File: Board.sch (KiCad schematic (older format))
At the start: 0 parts

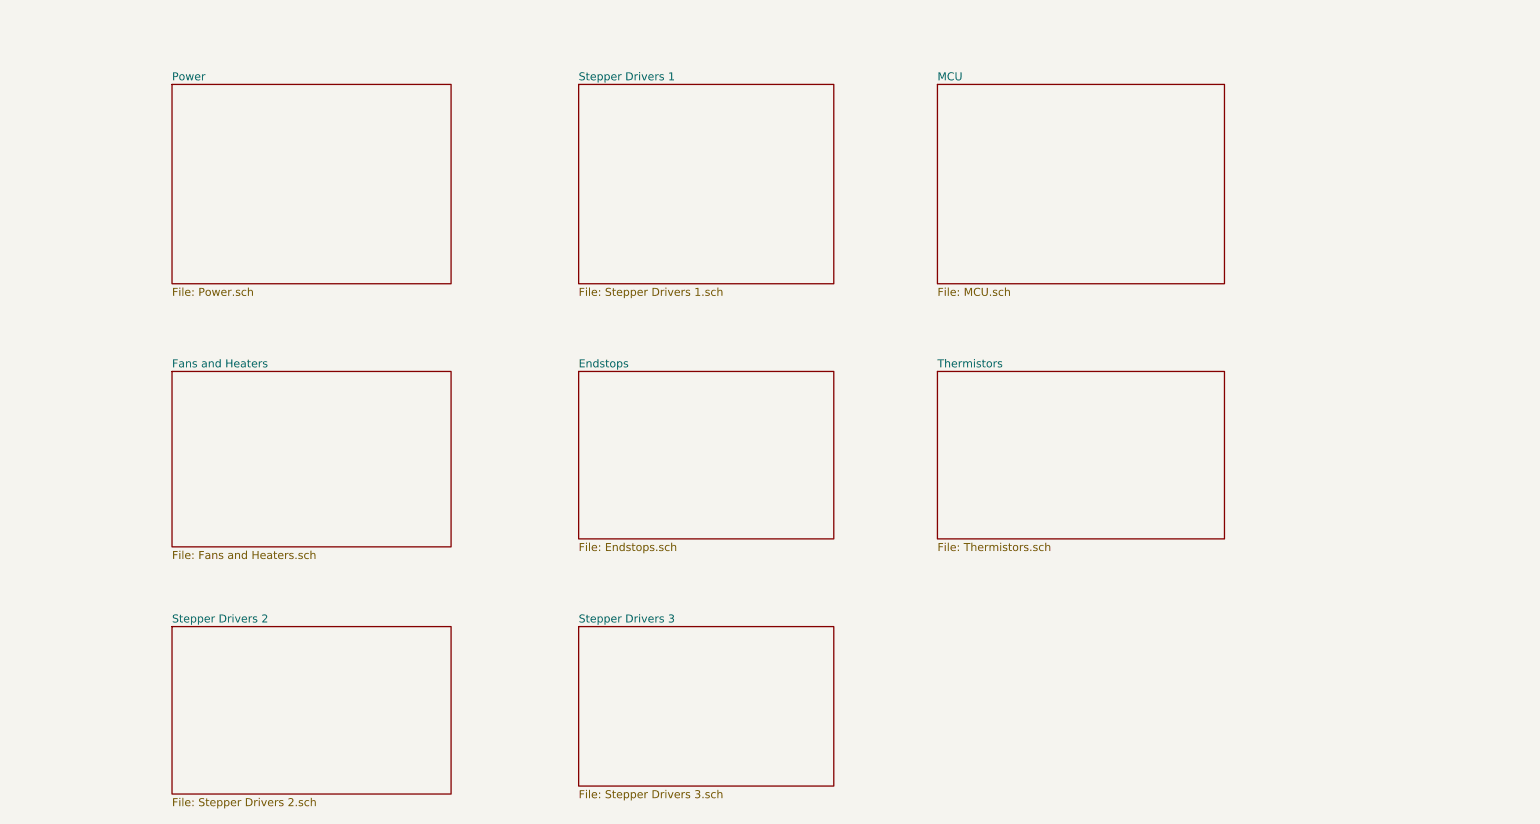
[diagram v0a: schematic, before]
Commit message: Added more footprints
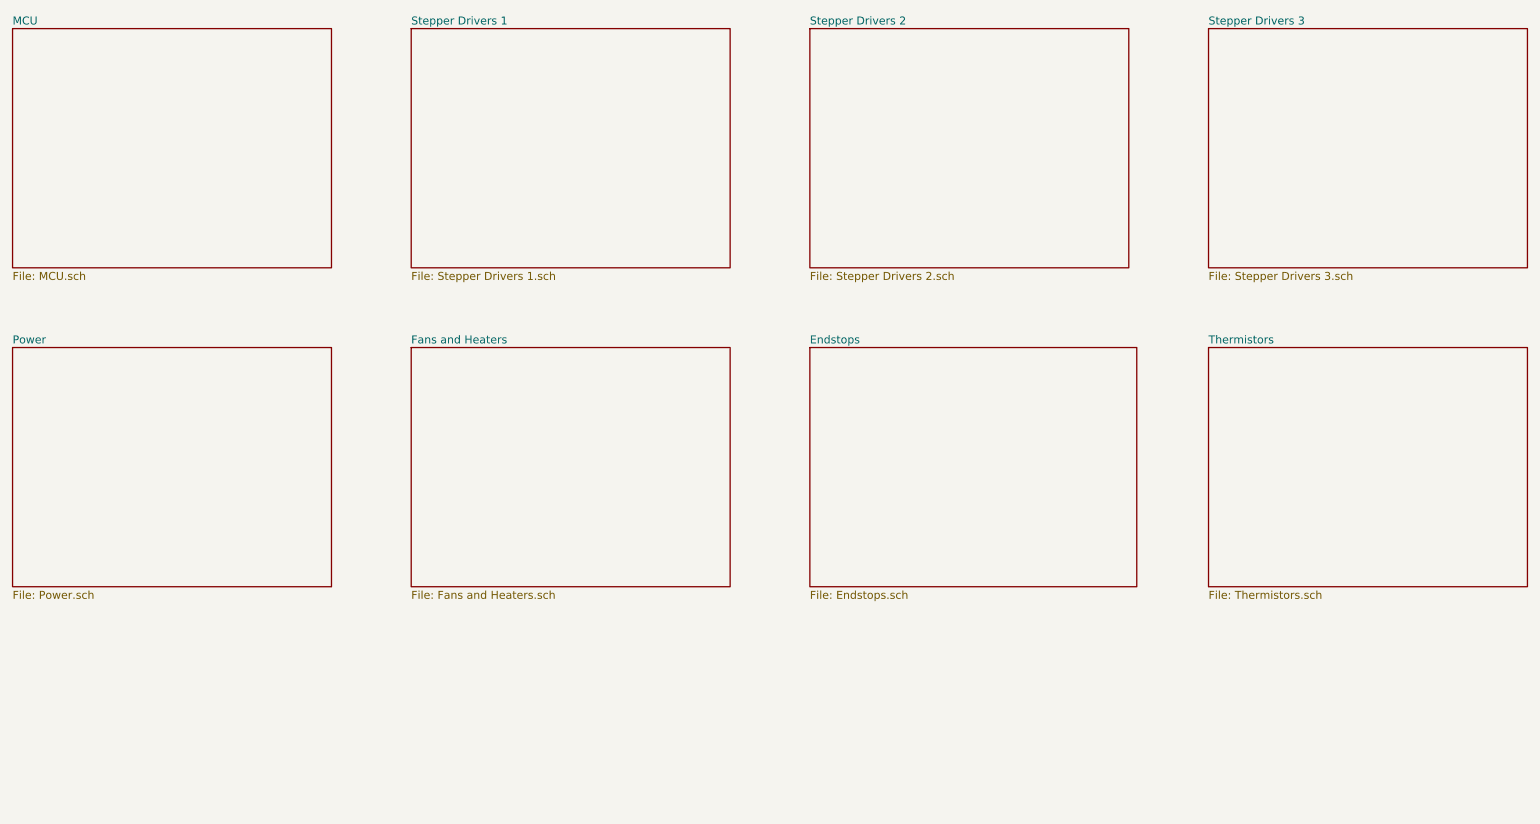
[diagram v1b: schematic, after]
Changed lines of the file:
@@
 $EndDescr
 $Sheet
-S 2000 1350 1750 1250
+S 1000 3000 2000 1500
 U 5F93246D
 F0 "Power" 50
@@
 $EndSheet
 $Sheet
-S 4550 1350 1600 1250
-U 5F93253C
-F0 "Stepper Drivers 1" 50
-F1 "Stepper Drivers 1.sch" 50
-$EndSheet
-$Sheet
-S 6800 1350 1800 1250
+S 1000 1000 2000 1500
 U 5F932656
 F0 "MCU" 50
@@
 $EndSheet
 $Sheet
-S 2000 3150 1750 1100
+S 3500 3000 2000 1500
 U 5F932696
 F0 "Fans and Heaters" 50
@@
 $EndSheet
 $Sheet
-S 4550 3150 1600 1050
+S 6000 3000 2050 1500
 U 5F9326CE
 F0 "Endstops" 50
@@
 $EndSheet
 $Sheet
-S 6800 3150 1800 1050
+S 8500 3000 2000 1500
 U 5F93273E
 F0 "Thermistors" 50
@@
 $EndSheet
 $Sheet
-S 2000 4750 1750 1050
+S 8500 1000 2000 1500
+U 5FB57E25
+F0 "Stepper Drivers 3" 50
+F1 "Stepper Drivers 3.sch" 50
+$EndSheet
+$Sheet
+S 6000 1000 2000 1500
 U 5FB57DE9
 F0 "Stepper Drivers 2" 50
@@
 $EndSheet
 $Sheet
-S 4550 4750 1600 1000
-U 5FB57E25
-F0 "Stepper Drivers 3" 50
-F1 "Stepper Drivers 3.sch" 50
+S 3500 1000 2000 1500
+U 5F93253C
+F0 "Stepper Drivers 1" 50
+F1 "Stepper Drivers 1.sch" 50
 $EndSheet
 $EndSCHEMATC
